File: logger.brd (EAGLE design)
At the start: 99 x 44.1 mm, 74 parts, among them IC1 LTC4412, J1 POWER_JACKPTH, Q1 FDN360P, Q2 FDN360P, Q3 2N7002PW, Q4 2N7002PW, Q5 2N7002PW, U3 FT231XS

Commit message: Improved board, modified and consolidated some components
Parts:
- C14, C15: device rc-master-smd:CECJ-0805 -> rc-master-smd:CECJ-1206
- C17, C18, C19, C20: device SparkFun-Capacitors:0402-CAP -> resistor:C0603
- C_LDO_SD, C_LDO_SENSE: value >=2.2uF -> 2.2uF
- DECOUP: value >=1uF -> 2.2uF
- LED1: value RED -> Yellow
- LED2: value YELLOW -> Blue
- PU1, PU2, PU3, PU4: value 3K -> 3k
- R11, R12: device SparkFun-Resistors:0402-RES -> resistor:R0603
- R13, R14, R15: device SparkFun-Passives:0402-RES -> resistor:R0603
- RCKL1, RCLK2: value 220ohm -> 220
- RX_SW1, TX_SW1: value 1Kohm -> 1k
- R_LED: value 330 -> 220; device rcl:R0603@1 -> resistor:R0603
- R_REF_A0: value Therm -> (none)
- R_RESET: value 10K -> 10k
- moved L_LPF 35.1 mm to (13.0, 2.54)
- moved C14 23.4 mm to (43.9, 14.0), turned to 0 degrees
- moved R13 19.4 mm to (96.0, 20.1), turned to 0 degrees
- moved R14 18.0 mm to (88.9, 20.1), turned to 0 degrees
- moved RCLK2 11.9 mm to (75.2, 34.1), turned to 90 degrees
- moved RCKL1 7.01 mm to (71.5, 25.5), turned to 0 degrees
- moved D1 3.61 mm to (67.7, 26.5)
- moved R11 3.35 mm to (88.9, 1.91), turned to 90 degrees
- moved DECOUP 3.17 mm to (94.0, 33.0)
- moved R15 1.42 mm to (86.0, 20.5)
- moved CLOCK_BATT_DECOUP 0.98 mm to (96.1, 33.0)
- moved C20 0.64 mm to (83.9, 21.5)
- moved COUT 0.45 mm to (97.5, 36.5)
- moved LED1 0.45 mm to (91.0, 2.52)
- moved LOGO1 0.45 mm to (83.3, 25.4)
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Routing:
- net D3-INT1: track 40.3 -> 130.4 mm, vias 2 -> 1
- net A6: track 171.0 -> 81.5 mm, vias 3 -> 5
- net X0: track 87.1 -> 31.0 mm, vias 5 -> 3
- net A2: track 120.9 -> 75.1 mm, vias 4 -> 2
- net A3: track 75.1 -> 113.7 mm
- net VDD: track 115.5 -> 150.5 mm, vias 7 -> 8
- net RXLED-: track 1.52 -> 35.0 mm
- net SDA: track 94.7 -> 64.8 mm, vias 3 -> 6
- net RESET: track 116.6 -> 91.3 mm
- net AVCC: track 47.0 -> 28.3 mm, vias 5 -> 0
- net N$2: track 19.3 -> 3.62 mm
- net TXLED-: track 4.55 -> 20.2 mm
- net CLK: track 69.4 -> 84.4 mm, vias 5 -> 3
- net D4-SENSE_3V3_SWITCH: track 53.5 -> 40.3 mm
- net X1: track 44.7 -> 57.5 mm, vias 4 -> 3
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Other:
- board text added: "Rx"
- board text added: "Tx"

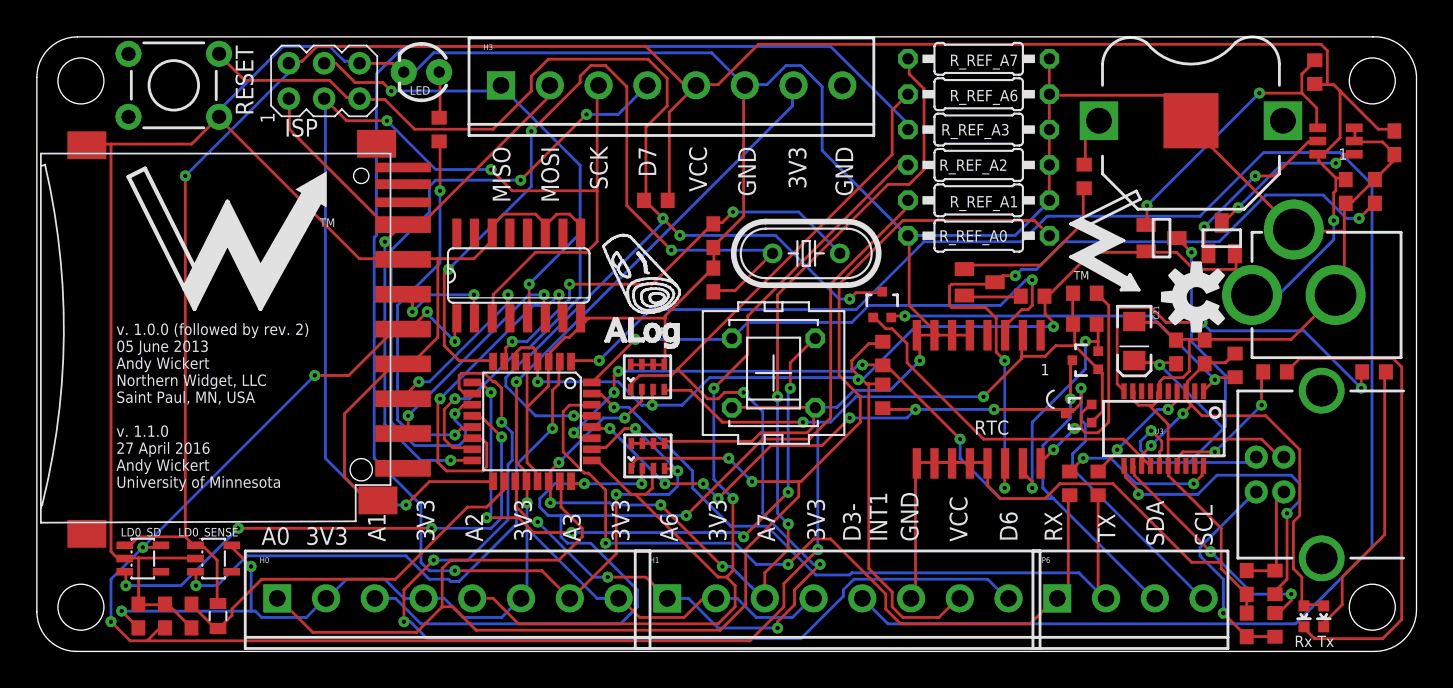
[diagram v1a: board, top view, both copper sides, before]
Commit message: Rmv via at screw hole
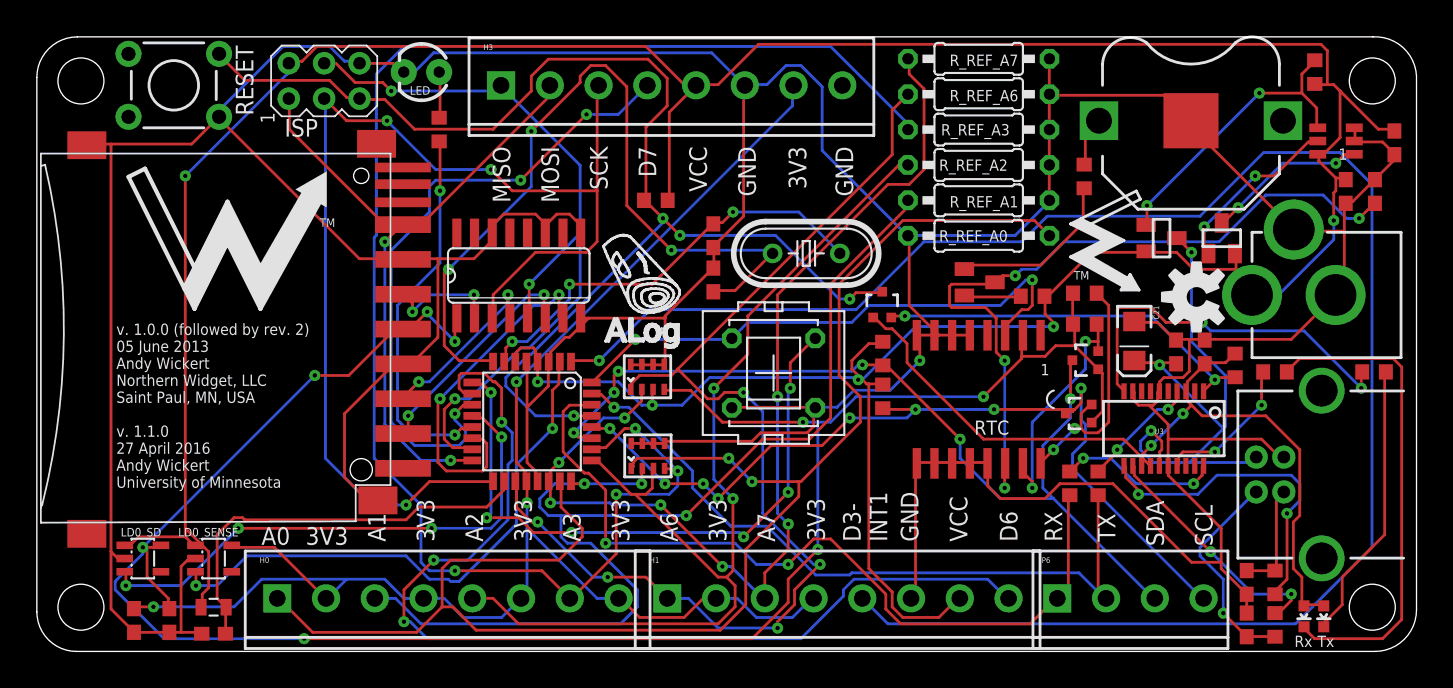
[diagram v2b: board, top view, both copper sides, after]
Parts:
- moved ADECOUP 2.03 mm to (12.7, 1.27), turned to 180 degrees
- moved L_LPF 0.71 mm to (12.7, 3.17), turned to 0 degrees
- moved C_LDO_SD 0.45 mm to (9.53, 2.22), turned to 90 degrees
- moved C_LDO_SENSE 0.45 mm to (6.99, 2.22), turned to 90 degrees
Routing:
- net GND: track 417.7 -> 422.0 mm
- net +3V3: track 109.3 -> 111.4 mm, vias 4 -> 3
- net AVCC: track 28.3 -> 30.1 mm
- net VDD: track 150.5 -> 152.0 mm
- net VCC: track 263.6 -> 265.0 mm

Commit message: Return to classic FTDI USB/serial
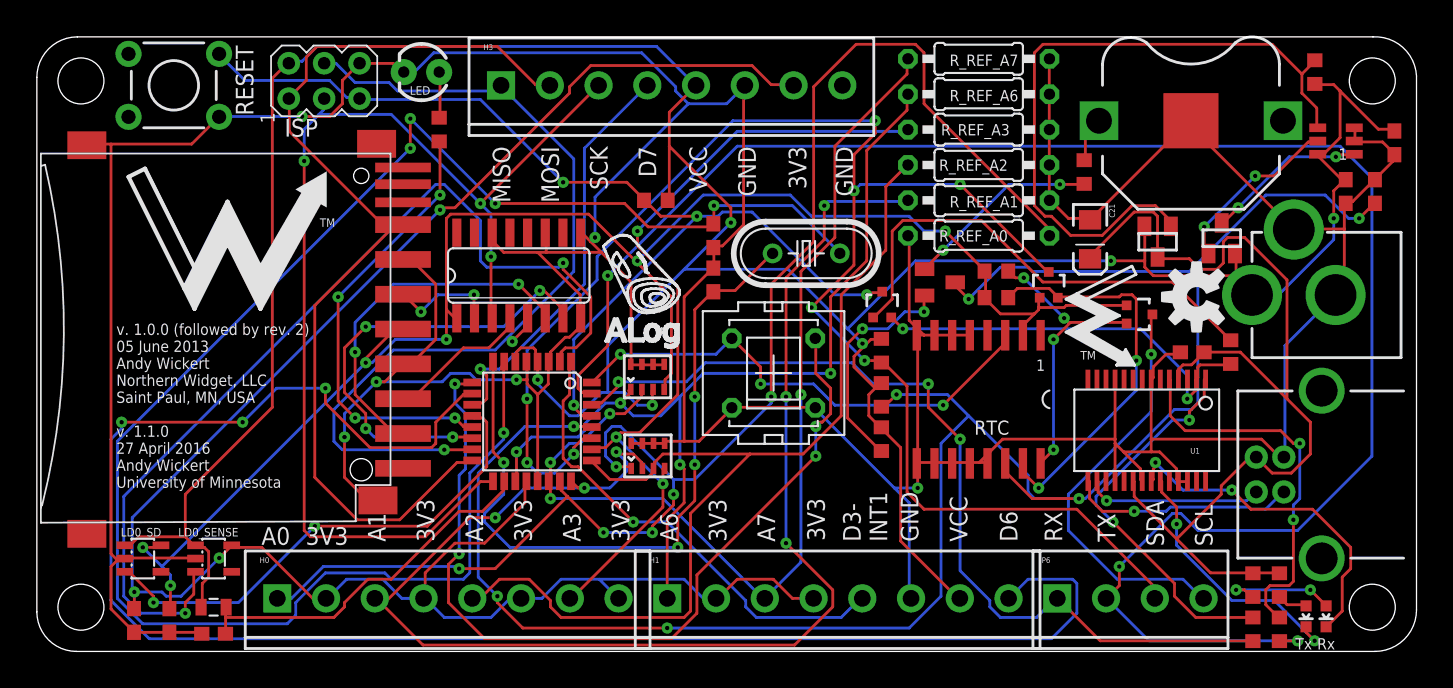
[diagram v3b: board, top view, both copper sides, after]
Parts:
- removed C18, C19: 47pF, resistor:C0603
- removed C20: 0.1uF, resistor:C0603
- removed R11, R12: 27ohm, resistor:R0603
- removed U3: FT231XS, SparkFun-DigitalIC:SSOP20_L
- added U1: FT232RL, SparkFun-DigitalIC:SSOP28DB
- PU1, PU2, PU3, PU4, RCKL1, RCLK2, RSTAT, RX_SW1, R_RESET, TX_SW1: device rcl:R0603@1 -> rcl:R0603
- moved RX_SW1 16.8 mm to (87.3, 1.59)
- moved R13 16.7 mm to (89.2, 4.76), turned to 270 degrees
- moved TX_SW1 16.7 mm to (89.2, 1.59)
- moved R14 15.4 mm to (87.3, 4.76), turned to 270 degrees
- moved RCKL1 14.9 mm to (60.6, 15.2), turned to 90 degrees
- moved Q4 8.35 mm to (79.2, 24.2), turned to 270 degrees
- moved C21 7.96 mm to (75.6, 29.6)
- moved PU3 6.63 mm to (68.9, 25.4)
- moved PU4 6.55 mm to (68.9, 27.3)
- moved Q3 6.01 mm to (72.7, 26.3), turned to 0 degrees
- moved U$3 5.41 mm to (76.8, 24.1)
- moved D1 2.86 mm to (64.8, 26.5)
- moved LED1 1.59 mm to (92.6, 2.52)
- moved LED2 1.27 mm to (91.1, 2.52)
- moved C17 1.16 mm to (83.0, 21.5), turned to 180 degrees
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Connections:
- removed net N$56: R11.2, U3.12
- removed net N$57: R12.1, U3.11
- removed net N$58: C18.1, JP5.D+, R12.2
- removed net N$59: C19.1, JP5.D-, R11.1
- removed net RXLED: R14.1, U3.17
- removed net RXLED-: LED1.C, R14.2
- removed net TXLED: R13.1, U3.10
- removed net TXLED-: LED2.C, R13.2
- new net N$10: LED2.A, R13.2
- new net N$3: JP5.D+, U1.15
- new net N$4: JP5.D-, U1.16
- new net N$5: LED1.C, U1.22
- new net N$6: LED2.C, U1.23
- new net N$9: LED1.A, R14.2
- net 3.3V: no longer C20.1, LED1.A, LED2.A, U3.13, U3.14, U3.3
- net DTR: now also U1.2; no longer U3.1
- net GND: now also U1.11, U1.18, U1.21, U1.25, U1.26, U1.7; no longer C18.2, C19.2, C20.2, U3.16, U3.6, U3.9
- net N$27: now also U1.1; no longer U3.20
- net N$29: now also U1.5; no longer U3.4
- net VUSB: now also R13.1, R14.1, U1.20, U1.4; no longer U3.15
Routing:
- net D3-INT1: track 130.4 -> 34.2 mm
- net X0: track 31.0 -> 124.7 mm, vias 3 -> 5
- net TX-O: track 51.6 -> 131.2 mm, vias 1 -> 3
- net A3: track 113.7 -> 60.2 mm, vias 4 -> 3
- net SDA: track 64.8 -> 117.7 mm, vias 6 -> 8
- net SCL: track 63.9 -> 114.1 mm, vias 8 -> 5
- net D6: track 73.8 -> 123.2 mm
- net RXLED-: track 35.0 -> 0.00 mm
- net VDD: track 152.0 -> 117.9 mm, vias 8 -> 6
- net VCC: track 265.0 -> 233.6 mm
- net VUSB: track 41.8 -> 73.1 mm, vias 3 -> 0
- net D4-SENSE_3V3_SWITCH: track 40.3 -> 69.8 mm
- net +3V3: track 111.4 -> 139.7 mm
- net N$7: track 21.6 -> 49.4 mm, vias 2 -> 0
- net TXLED: track 27.2 -> 0.00 mm, vias 2 -> 0
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
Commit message: replace logger with logger_Chad
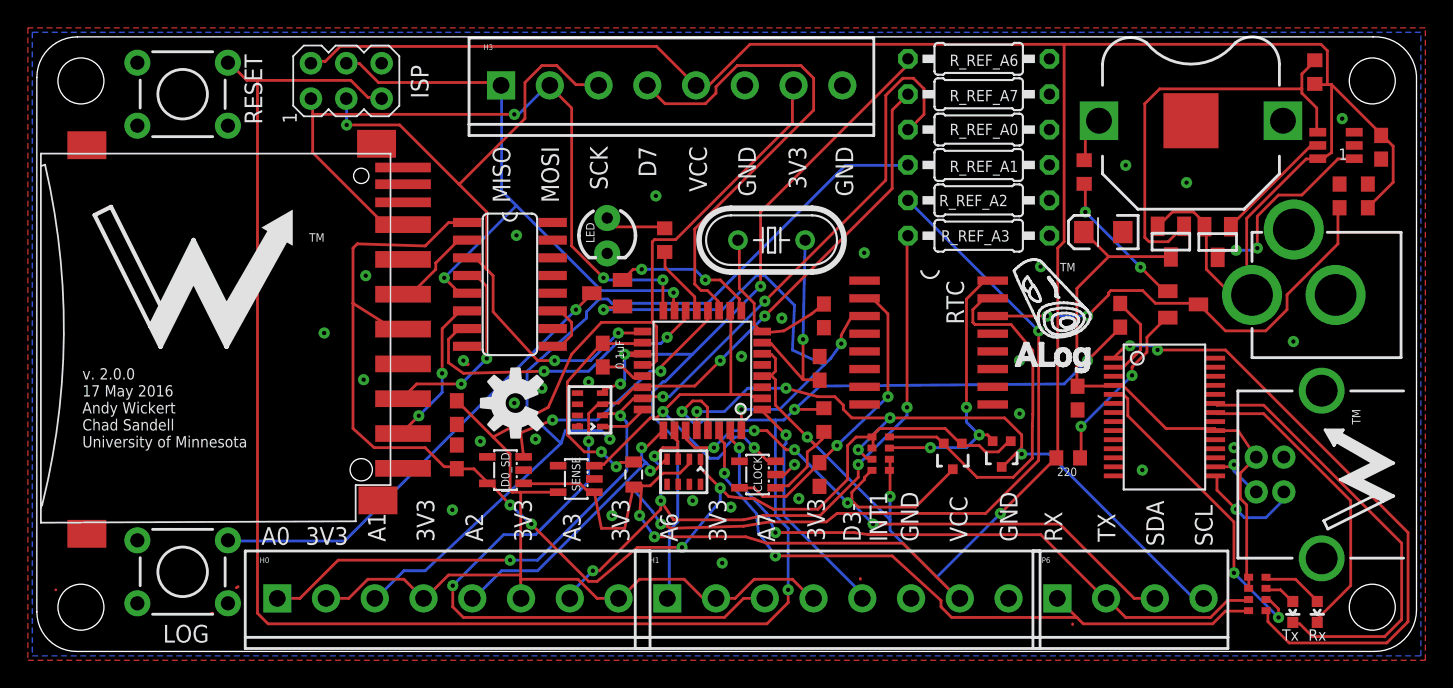
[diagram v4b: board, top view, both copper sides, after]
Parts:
- removed LD0_SENSE: LP2985, adafruit:SOT23-5L
- removed MANUAL_LOG: Log Now, switch-misc:PVA1F
- removed PU1, PU2, PU3, PU4: 3k, rcl:R0603
- removed Q5: 2N7002PW, SparkFun-DiscreteSemi:SOT323
- removed R13, R14: 1k, resistor:R0603
- removed R15: 10k, resistor:R0603
- removed RX_SW1, TX_SW1: 1k, rcl:R0603
- added CLOCK, SENSE: LP2985, adafruit:SOT23-5L
- added COUT1: 1uF, rcl:C0603
- added C_LDO_SENSE1: 2.2uF, resistor:C0603
- added D2: BAT54C, semicon-smd-ipc:SOT23C
- added LOG: LOG, SparkFun-Electromechanical:TACTILE-PTH
- added RN1: 1K, resistor-dil:0603-ARC
- added RN2: 3.3K, resistor-dil:0603-ARC
- moved LOGO1 49.5 mm to (34.4, 17.8)
- moved ADECOUP 34.4 mm to (40.6, 21.3), turned to 270 degrees
- moved L_LPF 31.6 mm to (42.9, 12.7), turned to 90 degrees
- moved U$2 29.5 mm to (73.0, 25.3)
- moved C_LDO_SENSE 27.6 mm to (30.2, 17.1)
- moved LD0_SD 26.8 mm to (33.7, 13.0), turned to 90 degrees
- moved C_LDO_SD 23.7 mm to (30.2, 14.0), turned to 270 degrees
- moved U$3 21.2 mm to (94.5, 12.3), turned to 90 degrees
- moved R_RESET 19.9 mm to (56.5, 16.6), turned to 270 degrees
- moved R_LED 18.0 mm to (45.1, 29.5)
- moved LED 17.8 mm to (41.0, 29.8), turned to 270 degrees
- moved D1 17.5 mm to (82.3, 24.9)
- moved Q3 14.1 mm to (65.8, 14.0), turned to 180 degrees
- moved Q4 14.1 mm to (69.3, 14.2), turned to 180 degrees
- moved RCKL1 13.5 mm to (74.1, 13.9), turned to 180 degrees
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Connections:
- net D9-LED renamed D9_LED
- removed net 3.3V: Q5.1, R15.2
- removed net D4-SENSE_3V3_SWITCH: LD0_SENSE.3, MCU.2
- removed net D6: H1.8, MCU.10
- new net D6-CLOCK_3V3_SWITCH: CLOCK.3, MCU.10, MCU.2, SENSE.3
- new net N$11: D2.3, LOG.3
- new net VCL: CLOCK.5, C_LDO_SENSE1.2, RTC.2
- net +3V3: now also SENSE.5; no longer LD0_SENSE.5
- net A0: now also C15.B1; no longer C14.A1
- net A1: now also C15.A1; no longer C14.B1
- net A2: now also C14.D1; no longer C14.C1
- net A3: now also C14.C1; no longer C14.D1
- net A6: now also C15.D1; no longer C15.A1
- net A7: now also C15.C1; no longer C15.B1
- net D5_MANUAL_LOG: now also D2.2; no longer MANUAL_LOG.3
- net DTR: now also COUT1.1; no longer Q5.2, R15.1
- net GND: now also CLOCK.2, C_LDO_SENSE1.1, H1.8, H3.8, LOG.1, SENSE.2; no longer LD0_SENSE.2, MANUAL_LOG.2, MANUAL_LOG.4
- net INT0: now also D2.1; no longer MANUAL_LOG.1
- net N$10: now also RN1.3; no longer R13.2
- net N$27: now also RN1.1; no longer RX_SW1.1
- net N$29: now also RN1.2; no longer TX_SW1.1
- net N$9: now also RN1.4; no longer R14.2
- net RESET: now also COUT1.2; no longer Q5.3
- net RX-I: now also RN1.8; no longer RX_SW1.2
- net SCL: now also RN2.7; no longer PU2.1
- net SCL_3V3: now also RN2.3; no longer PU4.1
- net SDA: now also RN2.8; no longer PU1.1
- net SDA_3V3: now also RN2.4; no longer PU3.1
- net TX-O: now also RN1.7; no longer TX_SW1.2
- net VCC: now also C14.B1, CLOCK.1, RN2.1, RN2.2, SENSE.1; no longer C15.C1, LD0_SENSE.1, PU1.2, PU2.2
- net VDD: now also C14.A1, RN2.5, RN2.6; no longer C15.D1, PU3.2, PU4.2, RTC.2
- net VUSB: now also RN1.5, RN1.6; no longer R13.1, R14.1
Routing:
- net GND: track 396.2 -> 12.5 mm, vias 6 -> 30
- net D6: track 123.2 -> 0.00 mm, vias 3 -> 0
- net X0: track 124.7 -> 15.7 mm, vias 5 -> 1
- net TX-O: track 131.2 -> 45.5 mm, vias 3 -> 2
- net D4-SENSE_3V3_SWITCH: track 69.8 -> 0.00 mm, vias 2 -> 0
- net RESET: track 74.1 -> 143.5 mm
- net SDA: track 117.7 -> 51.8 mm, vias 8 -> 5
- net SCL: track 114.1 -> 52.0 mm
- net D5_MANUAL_LOG: track 61.8 -> 10.5 mm, vias 4 -> 2
- net X1: track 51.9 -> 12.4 mm, vias 4 -> 0
- net +3V3: track 139.7 -> 100.4 mm, vias 3 -> 0
- net 3.3V: track 35.0 -> 0.00 mm
- net A1: track 100.6 -> 66.7 mm, vias 6 -> 1
- net N$11: track 0.00 -> 33.5 mm, vias 0 -> 1
- net A0: track 107.1 -> 73.7 mm, vias 6 -> 4
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- added copper zone on layer 1, net GND
- added copper zone on layer 16, net GND
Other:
- board text added: "v. 2.0.0 17 May 2016 Andy Wickert Chad Sandell University of Minnesota"
- board text removed: "D6"
- board text removed: "v. 1.0.0 (followed by rev. 2) 05 June 2013 Andy Wickert Northern Widget, LLC Saint Paul, MN, USA v. 1.1.0 27 April 2016 Andy Wickert University of Minnesota"

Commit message: Added 5V boost from VCC to board
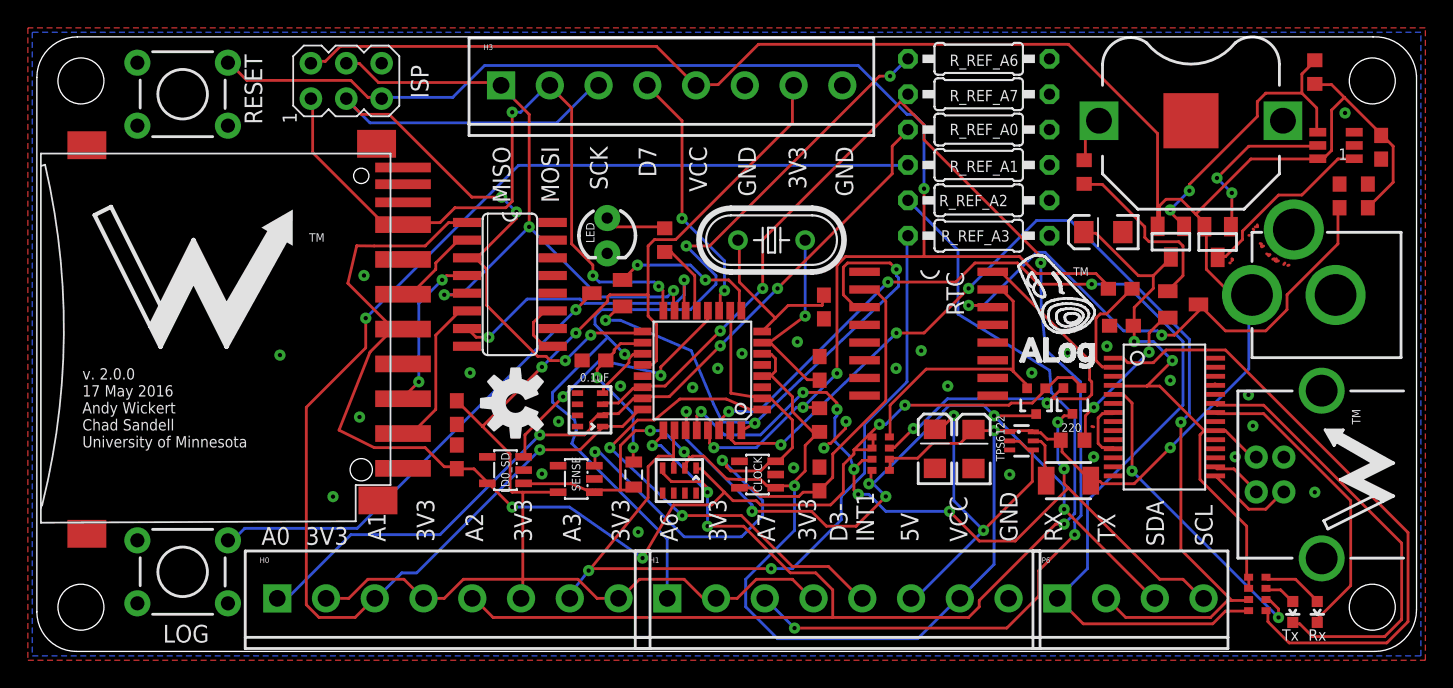
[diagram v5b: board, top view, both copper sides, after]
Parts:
- added C1, C2: 10uF, SparkFun-Passives:EIA3216
- added L1: 4.7uH, SteveMarple:1210
- added TPS6122: TPS6122TPS6122, csandell:SC70-6L
- moved Q3 7.18 mm to (71.8, 18.0)
- moved Q4 6.35 mm to (74.4, 18.0)
- moved C17 6.07 mm to (77.9, 23.4), turned to 180 degrees
- moved COUT1 1.91 mm to (77.8, 26.0), turned to 180 degrees
- moved RCKL1 1.31 mm to (74.4, 15.2)
- moved ADECOUP 0.74 mm to (40.0, 20.9), turned to 180 degrees
- moved C14 0.71 mm to (46.1, 12.3)
- moved CX1 0.64 mm to (56.5, 24.7)
- moved RTC 0.64 mm to (64.0, 22.8)
- moved U$2 0.45 mm to (73.3, 25.6)
- moved R_RESET 0.32 mm to (56.2, 16.6)
- moved C_LDO_SENSE1 0.32 mm to (56.2, 12.4), turned to 270 degrees
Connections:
- new net 5V: C2.A, H1.6, TPS6122.2, TPS6122.4
- new net N$12: L1.1, TPS6122.5
- net GND: now also C1.C, C2.C, TPS6122.3; no longer H1.6
- net VCC: now also C1.A, L1.2, TPS6122.1, TPS6122.6
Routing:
- net RESET: track 143.5 -> 105.6 mm
- net TX-O: track 45.5 -> 75.7 mm, vias 2 -> 4
- net A1: track 66.7 -> 96.6 mm, vias 1 -> 2
- net RX-I: track 49.0 -> 78.1 mm, vias 2 -> 3
- net 5V: track 0.00 -> 27.3 mm, vias 0 -> 2
- net A2: track 77.5 -> 101.9 mm
- net A7: track 78.3 -> 96.8 mm, vias 4 -> 5
- net D3-INT1: track 16.7 -> 35.0 mm, vias 1 -> 2
- net D7-CS-EXT: track 35.5 -> 18.6 mm, vias 0 -> 2
- net A0: track 73.7 -> 60.7 mm, vias 4 -> 3
- net VCC: track 245.6 -> 234.9 mm
- net A6: track 57.9 -> 67.2 mm
- net N$7: track 30.7 -> 21.4 mm, vias 0 -> 2
- net D6-CLOCK_3V3_SWITCH: track 31.4 -> 40.6 mm
- net SCL_3V3: track 20.6 -> 29.7 mm, vias 3 -> 2
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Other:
- board text added: "5V"
